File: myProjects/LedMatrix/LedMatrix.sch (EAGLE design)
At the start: 8 parts, among them IC1 74HC595N, IC2 74HC595N, IC3 74HC595N

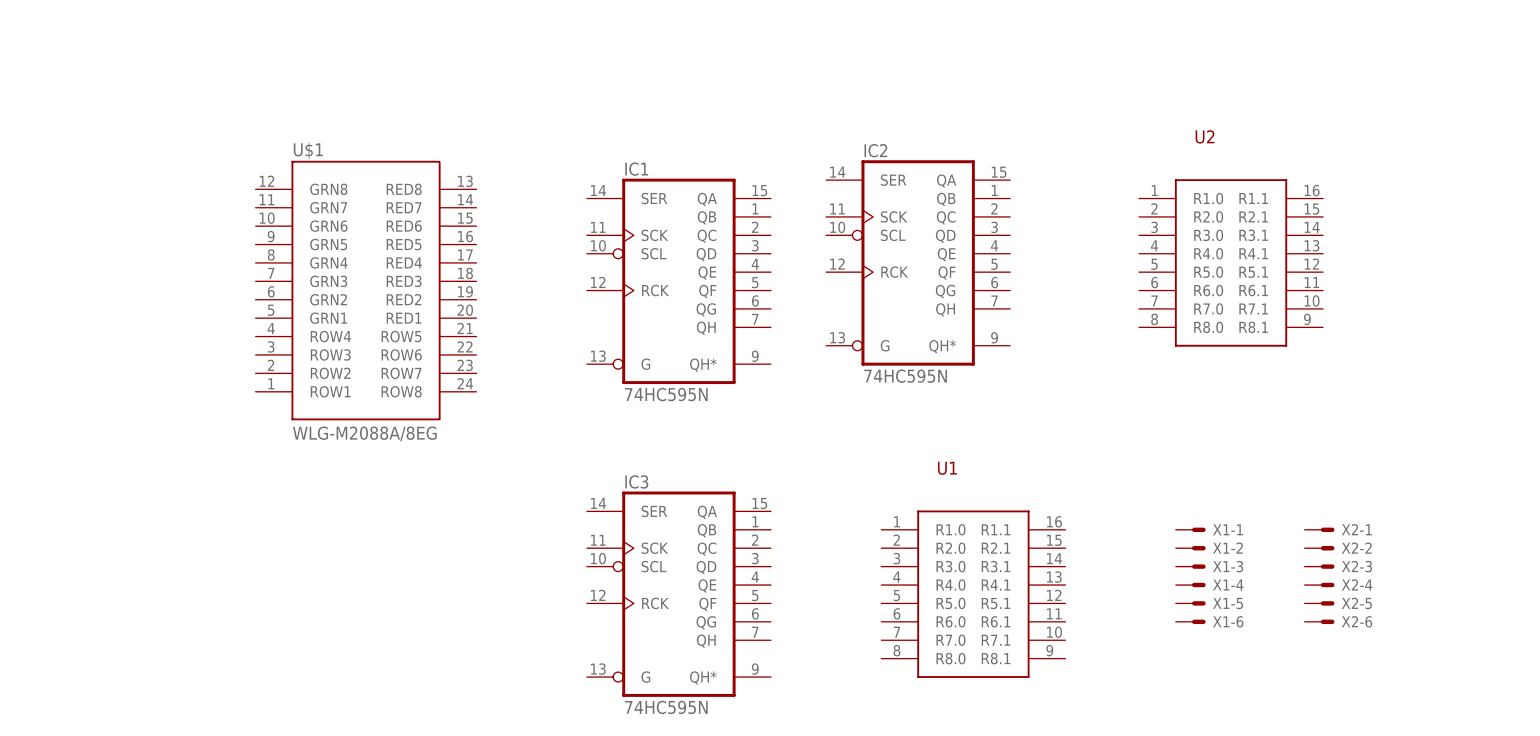
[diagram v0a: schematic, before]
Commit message: completed board for led matrix
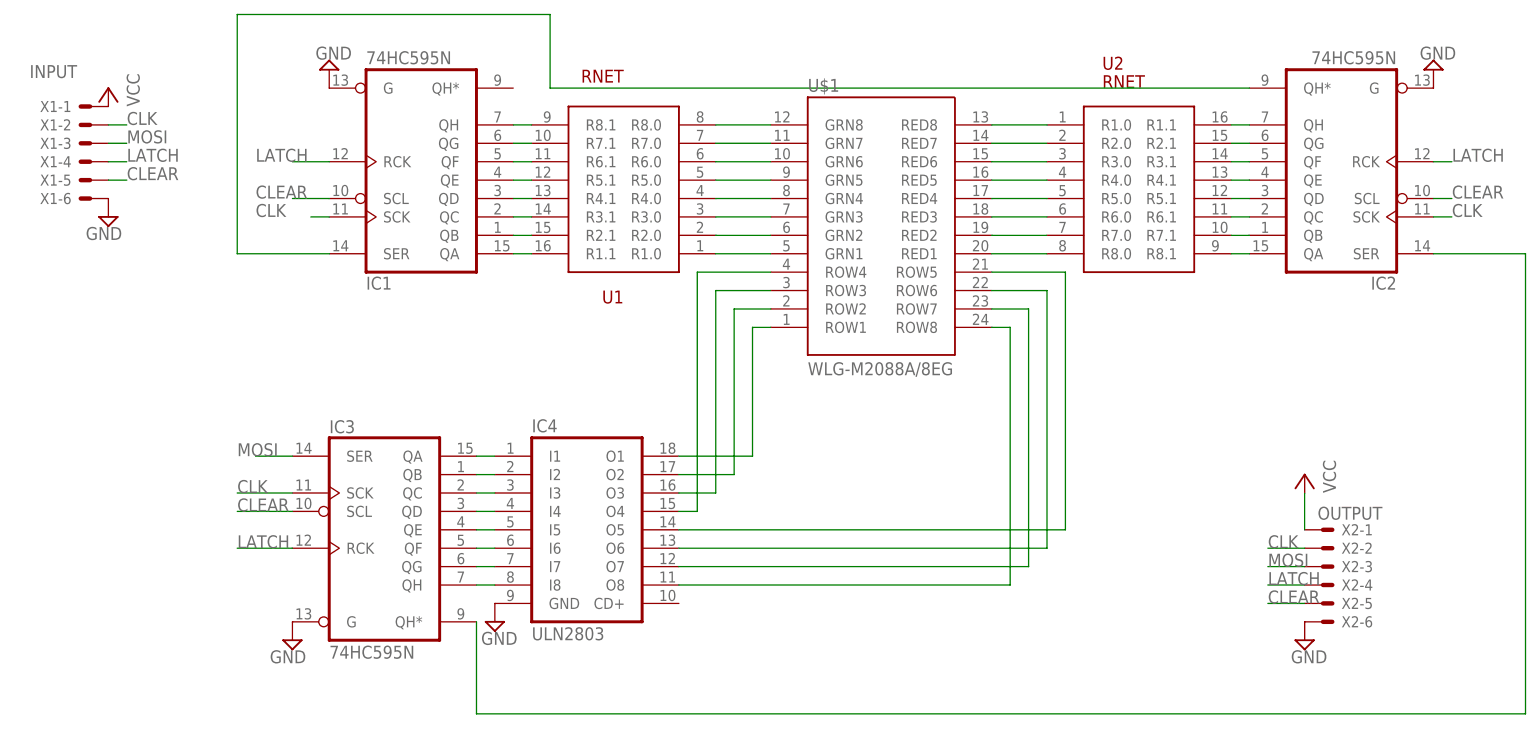
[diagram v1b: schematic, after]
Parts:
- added IC4: ULN2803, uln-udn:ULN2803A
- U1, U2: value (none) -> RNET
- X1: value (none) -> INPUT
- X2: value (none) -> OUTPUT
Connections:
- new net CLEAR: IC1A.SCL, IC2A.SCL, IC3A.SCL, X1-5.S, X2-5.S
- new net CLK: IC1A.SCK, IC2A.SCK, IC3A.SCK, X1-2.S, X2-2.S
- new net GND: IC1A.G, IC2A.G, IC3A.G, IC4.GND, X1-6.S, X2-6.S
- new net LATCH: IC1A.RCK, IC2A.RCK, IC3A.RCK, X1-4.S, X2-4.S
- new net MOSI: IC3A.SER, X1-3.S, X2-3.S
- new net N$1: IC1A.QB, U1.R2.1
- new net N$10: U$1.GRN2, U1.R2.0
- new net N$11: U$1.GRN3, U1.R3.0
- new net N$12: U$1.GRN4, U1.R4.0
- new net N$13: U$1.GRN5, U1.R5.0
- new net N$14: U$1.GRN6, U1.R6.0
- new net N$15: U$1.GRN7, U1.R7.0
- new net N$16: U$1.GRN8, U1.R8.0
- new net N$17: U$1.RED8, U2.R1.0
- new net N$18: U$1.RED7, U2.R2.0
- new net N$19: U$1.RED6, U2.R3.0
- new net N$2: IC1A.QC, U1.R3.1
- new net N$20: U$1.RED5, U2.R4.0
- new net N$21: U$1.RED4, U2.R5.0
- new net N$22: U$1.RED3, U2.R6.0
- new net N$23: U$1.RED2, U2.R7.0
- new net N$24: U$1.RED1, U2.R8.0
- new net N$25: IC2A.QB, U2.R7.1
- new net N$26: IC2A.QC, U2.R6.1
- new net N$27: IC2A.QD, U2.R5.1
- new net N$28: IC2A.QE, U2.R4.1
- new net N$29: IC2A.QF, U2.R3.1
- new net N$3: IC1A.QD, U1.R4.1
- new net N$30: IC2A.QG, U2.R2.1
- new net N$31: IC2A.QH, U2.R1.1
- new net N$32: IC2A.QA, U2.R8.1
- new net N$33: IC3A.QB, IC4.I2
- new net N$34: IC3A.QC, IC4.I3
- new net N$35: IC3A.QD, IC4.I4
- new net N$36: IC3A.QE, IC4.I5
- new net N$37: IC3A.QF, IC4.I6
- new net N$38: IC3A.QG, IC4.I7
- new net N$39: IC3A.QH, IC4.I8
- new net N$4: IC1A.QE, U1.R5.1
- new net N$40: IC3A.QA, IC4.I1
- new net N$41: IC4.O1, U$1.ROW1
- new net N$42: IC4.O2, U$1.ROW2
- new net N$43: IC4.O3, U$1.ROW3
- new net N$44: IC4.O4, U$1.ROW4
- new net N$45: IC4.O5, U$1.ROW5
- new net N$46: IC4.O6, U$1.ROW6
- new net N$47: IC4.O7, U$1.ROW7
- new net N$48: IC4.O8, U$1.ROW8
- new net N$49: IC2A.SER, IC3A.QH*
- new net N$5: IC1A.QF, U1.R6.1
- new net N$50: IC1A.SER, IC2A.QH*
- new net N$6: IC1A.QG, U1.R7.1
- new net N$7: IC1A.QH, U1.R8.1
- new net N$8: IC1A.QA, U1.R1.1
- new net N$9: U$1.GRN1, U1.R1.0
- new net VCC: X1-1.S, X2-1.S
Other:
- moved on the sheet: IC1, IC2, IC3, U$1, U1, U2, X1-1, X1-2, X1-3, X1-4, X1-5, X1-6

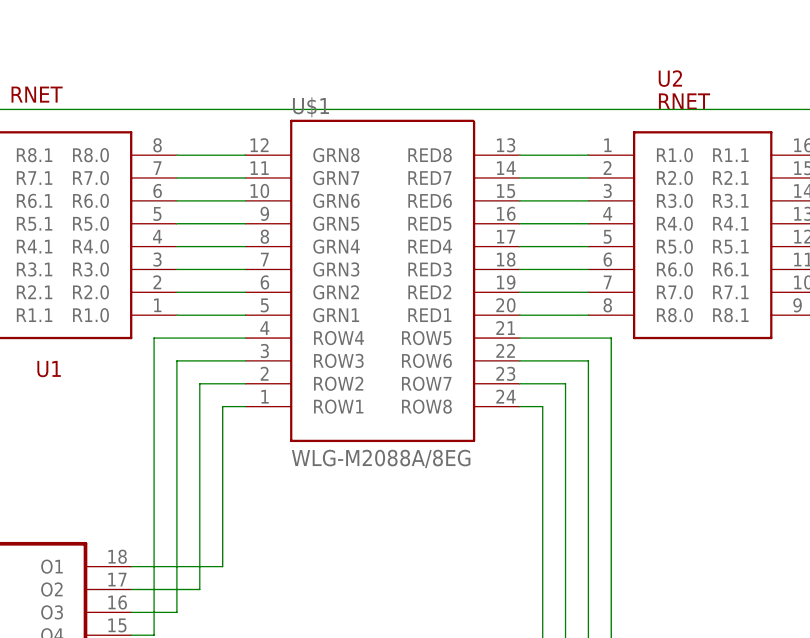
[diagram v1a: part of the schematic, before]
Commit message: fixed some labelling
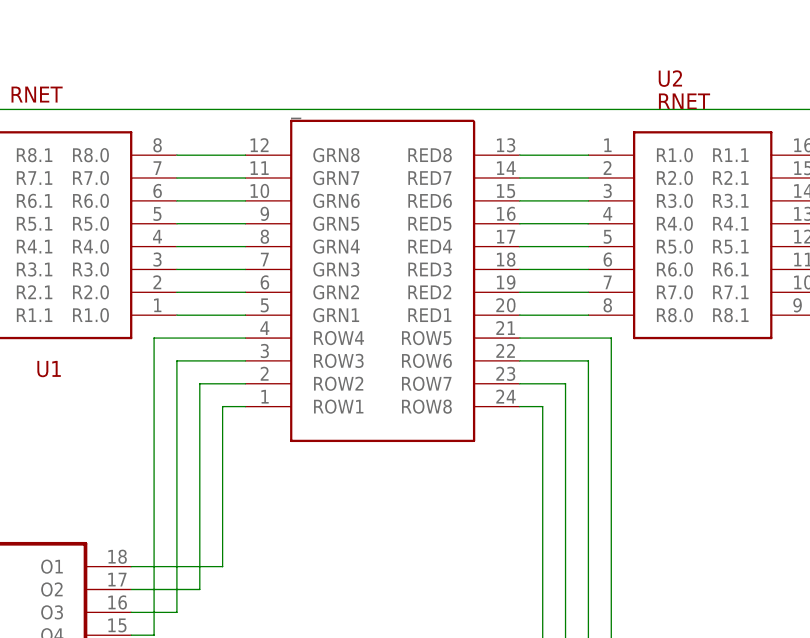
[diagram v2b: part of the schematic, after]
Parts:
- renumbered U$1 to _
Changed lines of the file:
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@@
 </classes>
 <parts>
-<part name="U$1" library="led-matrix-v2" deviceset="WLG-M2088A" device="/8EG"/>
+<part name="_" library="led-matrix-v2" deviceset="WLG-M2088A" device="/8EG" value=""/>
 <part name="IC1" library="74xx-eu" deviceset="74*595" device="N" technology="HC"/>
 <part name="IC2" library="74xx-eu" deviceset="74*595" device="N" technology="HC"/>
@@
 </plain>
 <instances>
-<instance part="U$1" gate="G$1" x="93.98" y="69.85"/>
+<instance part="_" gate="G$1" x="93.98" y="69.85"/>
 <instance part="IC1" gate="A" x="30.48" y="76.2" rot="MR180"/>
 <instance part="IC2" gate="A" x="157.48" y="76.2" rot="R180"/>
@@
 <net name="N$9" class="0">
 <segment>
-<pinref part="U$1" gate="G$1" pin="GRN1"/>
+<pinref part="_" gate="G$1" pin="GRN1"/>
 <pinref part="U1" gate="G$1" pin="R1.0"/>
 <wire x1="71.12" y1="66.04" x2="78.74" y2="66.04" width="0.1524" layer="91"/>
@@
 <net name="N$10" class="0">
 <segment>
-<pinref part="U$1" gate="G$1" pin="GRN2"/>
+<pinref part="_" gate="G$1" pin="GRN2"/>
 <pinref part="U1" gate="G$1" pin="R2.0"/>
 <wire x1="71.12" y1="68.58" x2="78.74" y2="68.58" width="0.1524" layer="91"/>
@@
 <net name="N$11" class="0">
 <segment>
-<pinref part="U$1" gate="G$1" pin="GRN3"/>
+<pinref part="_" gate="G$1" pin="GRN3"/>
 <pinref part="U1" gate="G$1" pin="R3.0"/>
 <wire x1="71.12" y1="71.12" x2="78.74" y2="71.12" width="0.1524" layer="91"/>
@@
 <net name="N$12" class="0">
 <segment>
-<pinref part="U$1" gate="G$1" pin="GRN4"/>
+<pinref part="_" gate="G$1" pin="GRN4"/>
 <pinref part="U1" gate="G$1" pin="R4.0"/>
 <wire x1="71.12" y1="73.66" x2="78.74" y2="73.66" width="0.1524" layer="91"/>
@@
 <net name="N$13" class="0">
 <segment>
-<pinref part="U$1" gate="G$1" pin="GRN5"/>
+<pinref part="_" gate="G$1" pin="GRN5"/>
 <pinref part="U1" gate="G$1" pin="R5.0"/>
 <wire x1="71.12" y1="76.2" x2="78.74" y2="76.2" width="0.1524" layer="91"/>
@@
 <net name="N$14" class="0">
 <segment>
-<pinref part="U$1" gate="G$1" pin="GRN6"/>
+<pinref part="_" gate="G$1" pin="GRN6"/>
 <pinref part="U1" gate="G$1" pin="R6.0"/>
 <wire x1="71.12" y1="78.74" x2="78.74" y2="78.74" width="0.1524" layer="91"/>
@@
 <net name="N$15" class="0">
 <segment>
-<pinref part="U$1" gate="G$1" pin="GRN7"/>
+<pinref part="_" gate="G$1" pin="GRN7"/>
 <pinref part="U1" gate="G$1" pin="R7.0"/>
 <wire x1="71.12" y1="81.28" x2="78.74" y2="81.28" width="0.1524" layer="91"/>
@@
 <net name="N$16" class="0">
 <segment>
-<pinref part="U$1" gate="G$1" pin="GRN8"/>
+<pinref part="_" gate="G$1" pin="GRN8"/>
 <pinref part="U1" gate="G$1" pin="R8.0"/>
 <wire x1="71.12" y1="83.82" x2="78.74" y2="83.82" width="0.1524" layer="91"/>
@@
 <net name="N$17" class="0">
 <segment>
-<pinref part="U$1" gate="G$1" pin="RED8"/>
+<pinref part="_" gate="G$1" pin="RED8"/>
 <pinref part="U2" gate="G$1" pin="R1.0"/>
 <wire x1="116.84" y1="83.82" x2="109.22" y2="83.82" width="0.1524" layer="91"/>
@@
 <net name="N$18" class="0">
 <segment>
-<pinref part="U$1" gate="G$1" pin="RED7"/>
+<pinref part="_" gate="G$1" pin="RED7"/>
 <pinref part="U2" gate="G$1" pin="R2.0"/>
 <wire x1="116.84" y1="81.28" x2="109.22" y2="81.28" width="0.1524" layer="91"/>
@@
 <net name="N$19" class="0">
 <segment>
-<pinref part="U$1" gate="G$1" pin="RED6"/>
+<pinref part="_" gate="G$1" pin="RED6"/>
 <pinref part="U2" gate="G$1" pin="R3.0"/>
 <wire x1="116.84" y1="78.74" x2="109.22" y2="78.74" width="0.1524" layer="91"/>
@@
 <net name="N$20" class="0">
 <segment>
-<pinref part="U$1" gate="G$1" pin="RED5"/>
+<pinref part="_" gate="G$1" pin="RED5"/>
 <pinref part="U2" gate="G$1" pin="R4.0"/>
 <wire x1="116.84" y1="76.2" x2="109.22" y2="76.2" width="0.1524" layer="91"/>
@@
 <net name="N$21" class="0">
 <segment>
-<pinref part="U$1" gate="G$1" pin="RED4"/>
+<pinref part="_" gate="G$1" pin="RED4"/>
 <pinref part="U2" gate="G$1" pin="R5.0"/>
 <wire x1="116.84" y1="73.66" x2="109.22" y2="73.66" width="0.1524" layer="91"/>
@@
 <net name="N$22" class="0">
 <segment>
-<pinref part="U$1" gate="G$1" pin="RED3"/>
+<pinref part="_" gate="G$1" pin="RED3"/>
 <pinref part="U2" gate="G$1" pin="R6.0"/>
 <wire x1="116.84" y1="71.12" x2="109.22" y2="71.12" width="0.1524" layer="91"/>
@@
 <net name="N$23" class="0">
 <segment>
-<pinref part="U$1" gate="G$1" pin="RED2"/>
+<pinref part="_" gate="G$1" pin="RED2"/>
 <pinref part="U2" gate="G$1" pin="R7.0"/>
 <wire x1="116.84" y1="68.58" x2="109.22" y2="68.58" width="0.1524" layer="91"/>
@@
 <net name="N$24" class="0">
 <segment>
-<pinref part="U$1" gate="G$1" pin="RED1"/>
+<pinref part="_" gate="G$1" pin="RED1"/>
 <pinref part="U2" gate="G$1" pin="R8.0"/>
 <wire x1="116.84" y1="66.04" x2="109.22" y2="66.04" width="0.1524" layer="91"/>
@@
 <wire x1="66.04" y1="38.1" x2="76.2" y2="38.1" width="0.1524" layer="91"/>
 <wire x1="76.2" y1="38.1" x2="76.2" y2="55.88" width="0.1524" layer="91"/>
-<pinref part="U$1" gate="G$1" pin="ROW1"/>
+<pinref part="_" gate="G$1" pin="ROW1"/>
 <wire x1="76.2" y1="55.88" x2="78.74" y2="55.88" width="0.1524" layer="91"/>
 </segment>
@@
 <wire x1="66.04" y1="35.56" x2="73.66" y2="35.56" width="0.1524" layer="91"/>
 <wire x1="73.66" y1="35.56" x2="73.66" y2="58.42" width="0.1524" layer="91"/>
-<pinref part="U$1" gate="G$1" pin="ROW2"/>
+<pinref part="_" gate="G$1" pin="ROW2"/>
 <wire x1="73.66" y1="58.42" x2="78.74" y2="58.42" width="0.1524" layer="91"/>
 </segment>
@@
 <wire x1="66.04" y1="33.02" x2="71.12" y2="33.02" width="0.1524" layer="91"/>
 <wire x1="71.12" y1="33.02" x2="71.12" y2="60.96" width="0.1524" layer="91"/>
-<pinref part="U$1" gate="G$1" pin="ROW3"/>
+<pinref part="_" gate="G$1" pin="ROW3"/>
 <wire x1="71.12" y1="60.96" x2="78.74" y2="60.96" width="0.1524" layer="91"/>
 </segment>
@@
 <wire x1="66.04" y1="30.48" x2="68.58" y2="30.48" width="0.1524" layer="91"/>
 <wire x1="68.58" y1="30.48" x2="68.58" y2="63.5" width="0.1524" layer="91"/>
-<pinref part="U$1" gate="G$1" pin="ROW4"/>
+<pinref part="_" gate="G$1" pin="ROW4"/>
 <wire x1="68.58" y1="63.5" x2="78.74" y2="63.5" width="0.1524" layer="91"/>
 </segment>
@@
 <wire x1="66.04" y1="27.94" x2="119.38" y2="27.94" width="0.1524" layer="91"/>
 <wire x1="119.38" y1="27.94" x2="119.38" y2="63.5" width="0.1524" layer="91"/>
-<pinref part="U$1" gate="G$1" pin="ROW5"/>
+<pinref part="_" gate="G$1" pin="ROW5"/>
 <wire x1="119.38" y1="63.5" x2="109.22" y2="63.5" width="0.1524" layer="91"/>
 </segment>
@@
 <wire x1="66.04" y1="25.4" x2="116.84" y2="25.4" width="0.1524" layer="91"/>
 <wire x1="116.84" y1="25.4" x2="116.84" y2="60.96" width="0.1524" layer="91"/>
-<pinref part="U$1" gate="G$1" pin="ROW6"/>
+<pinref part="_" gate="G$1" pin="ROW6"/>
 <wire x1="116.84" y1="60.96" x2="109.22" y2="60.96" width="0.1524" layer="91"/>
 </segment>
@@
 <wire x1="66.04" y1="22.86" x2="114.3" y2="22.86" width="0.1524" layer="91"/>
 <wire x1="114.3" y1="22.86" x2="114.3" y2="58.42" width="0.1524" layer="91"/>
-<pinref part="U$1" gate="G$1" pin="ROW7"/>
+<pinref part="_" gate="G$1" pin="ROW7"/>
 <wire x1="114.3" y1="58.42" x2="109.22" y2="58.42" width="0.1524" layer="91"/>
 </segment>
@@
 <wire x1="66.04" y1="20.32" x2="111.76" y2="20.32" width="0.1524" layer="91"/>
 <wire x1="111.76" y1="20.32" x2="111.76" y2="55.88" width="0.1524" layer="91"/>
-<pinref part="U$1" gate="G$1" pin="ROW8"/>
+<pinref part="_" gate="G$1" pin="ROW8"/>
 <wire x1="111.76" y1="55.88" x2="109.22" y2="55.88" width="0.1524" layer="91"/>
 </segment>
